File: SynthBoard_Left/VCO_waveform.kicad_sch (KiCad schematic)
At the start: 24 parts, among them IC6 AS321KTR-G1, IC7 HEF4013BT,653, Q1 2SC1623(RANGE:300-400)

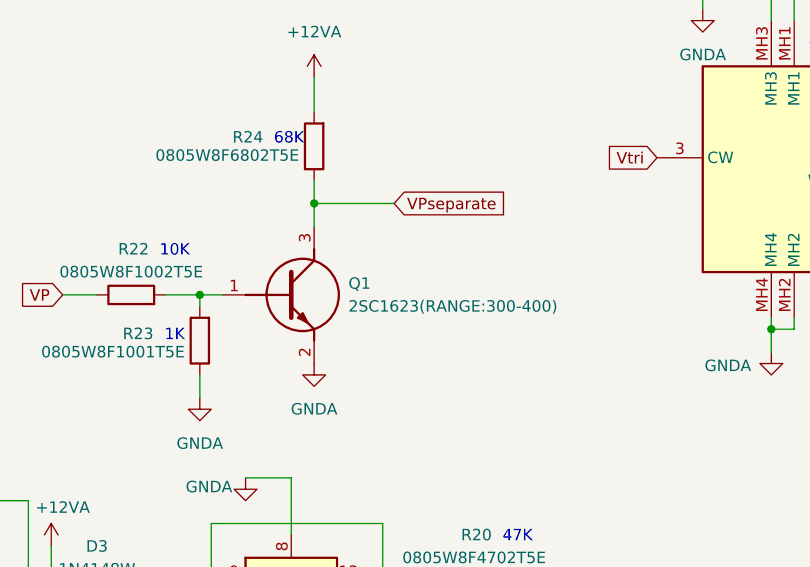
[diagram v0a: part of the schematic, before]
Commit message: SynthBoard_Left
JLCPCBでBasic部品に置き換えた
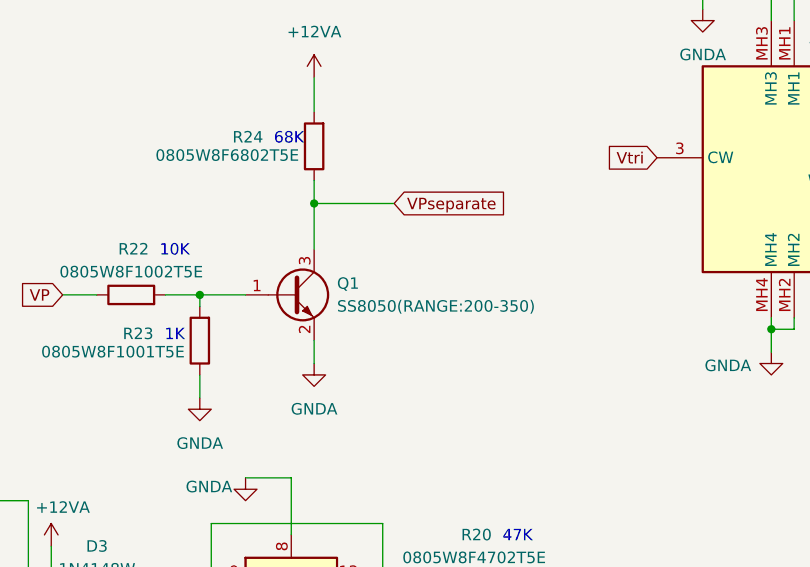
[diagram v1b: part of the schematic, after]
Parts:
- removed Q1: 2SC1623(RANGE:300-400), SamacSys_parts:SOT95P237X125-3N, symbol SamacSys_Parts:2SC1623-A
- added Q1: SS8050(RANGE:200-350), SamacSys_parts:SOT95P240X115-3N, symbol Transistor_BJT:SS8050
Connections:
- net GNDA: now also Q1.2 (E)
- net VPseparate: now also Q1.3 (C)
- net at R22.2, R23.2: now also Q1.1 (B)
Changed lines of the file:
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@@
 	(wire
 		(pts
-			(xy 105.41 90.17) (xy 105.41 92.71)
+			(xy 97.79 153.67) (xy 102.87 153.67)
 		)
 		(stroke
@@
 	(wire
 		(pts
-			(xy 97.79 153.67) (xy 102.87 153.67)
+			(xy 242.57 76.2) (xy 242.57 73.66)
 		)
 		(stroke
@@
 	(wire
 		(pts
-			(xy 242.57 76.2) (xy 242.57 73.66)
+			(xy 147.32 12.7) (xy 154.94 12.7)
 		)
 		(stroke
@@
 	(wire
 		(pts
-			(xy 147.32 12.7) (xy 154.94 12.7)
+			(xy 129.54 132.08) (xy 151.13 132.08)
 		)
 		(stroke
@@
 	(wire
 		(pts
-			(xy 129.54 132.08) (xy 151.13 132.08)
+			(xy 187.96 34.29) (xy 193.04 34.29)
 		)
 		(stroke
@@
 	(wire
 		(pts
-			(xy 187.96 34.29) (xy 193.04 34.29)
+			(xy 238.76 34.29) (xy 251.46 34.29)
 		)
 		(stroke
@@
 	(wire
 		(pts
-			(xy 238.76 34.29) (xy 251.46 34.29)
+			(xy 105.41 105.41) (xy 105.41 107.95)
 		)
 		(stroke
@@
 	(wire
 		(pts
-			(xy 92.71 100.33) (xy 95.25 100.33)
+			(xy 92.71 100.33) (xy 97.79 100.33)
 		)
 		(stroke
@@
 	(wire
 		(pts
+			(xy 105.41 90.17) (xy 105.41 95.25)
+		)
+		(stroke
+			(width 0)
+			(type default)
+		)
+	)
+	(wire
+		(pts
 			(xy 226.06 12.7) (xy 226.06 16.51)
 		)
@@
 	)
 	(symbol
-		(lib_id "SamacSys_Parts:2SC1623-A")
-		(at 95.25 100.33 0)
-		(unit 1)
-		(exclude_from_sim no)
-		(in_bom yes)
-		(on_board yes)
-		(dnp no)
-		(fields_autoplaced yes)
-		(property "Reference" "Q1"
-			(at 109.22 99.0599 0)
-			(effects
-				(font
-					(size 1.27 1.27)
-				)
-				(justify left)
-			)
-		)
-		(property "Value" "2SC1623(RANGE:300-400)"
-			(at 109.22 101.5999 0)
-			(effects
-				(font
-					(size 1.27 1.27)
-				)
-				(justify left)
-			)
-		)
-		(property "Footprint" "SamacSys_parts:SOT95P237X125-3N"
-			(at 109.22 201.6 0)
-			(effects
-				(font
-					(size 1.27 1.27)
-				)
-				(justify left top)
-				(hide yes)
-			)
-		)
-		(property "Datasheet" "https://www.mouser.in/datasheet/2/258/2SC1623_SOT_23_-1625845.pdf"
-			(at 109.22 301.6 0)
-			(effects
-				(font
-					(size 1.27 1.27)
-				)
-				(justify left top)
-				(hide yes)
-			)
-		)
-		(property "Description" "Renesas Electronics 2SC1623-A NPN Bipolar Transistor, 100 mA, 50 V, 3-Pin MiniMold"
-			(at 95.25 100.33 0)
-			(effects
-				(font
-					(size 1.27 1.27)
-				)
-				(hide yes)
-			)
-		)
-		(property "Height" "1.25"
-			(at 109.22 501.6 0)
-			(effects
-				(font
-					(size 1.27 1.27)
-				)
-				(justify left top)
-				(hide yes)
-			)
-		)
-		(property "Manufacturer_Name" "Renesas Electronics"
-			(at 109.22 601.6 0)
-			(effects
-				(font
-					(size 1.27 1.27)
-				)
-				(justify left top)
-				(hide yes)
-			)
-		)
-		(property "Manufacturer_Part_Number" "2SC1623-A"
-			(at 109.22 701.6 0)
-			(effects
-				(font
-					(size 1.27 1.27)
-				)
-				(justify left top)
-				(hide yes)
-			)
-		)
-		(property "Mouser Part Number" ""
-			(at 109.22 801.6 0)
-			(effects
-				(font
-					(size 1.27 1.27)
-				)
-				(justify left top)
-				(hide yes)
-			)
-		)
-		(property "Mouser Price/Stock" ""
-			(at 109.22 901.6 0)
-			(effects
-				(font
-					(size 1.27 1.27)
-				)
-				(justify left top)
-				(hide yes)
-			)
-		)
-		(property "Arrow Part Number" ""
-			(at 109.22 1001.6 0)
-			(effects
-				(font
-					(size 1.27 1.27)
-				)
-				(justify left top)
-				(hide yes)
-			)
-		)
-		(property "Arrow Price/Stock" ""
-			(at 109.22 1101.6 0)
-			(effects
-				(font
-					(size 1.27 1.27)
-				)
-				(justify left top)
-				(hide yes)
-			)
-		)
-		(pin "3"
-		)
-		(pin "2"
-		)
-		(pin "1"
-		)
-		(instances
-			(project "SynthBoard"
-				(path "/92765e2f-a998-485f-b610-76a9d5b50cba/54ae8d1b-caf5-4a85-9663-2a3f476f2243"
-					(reference "Q1")
-					(unit 1)
-				)
-			)
-		)
-	)
-	(symbol
 		(lib_id "SamacSys_Parts:PTA2043-2010CIB104")
 		(at 238.76 76.2 0)
@@
 					(unit 1)
 				)
+			)
+		)
+	)
+	(symbol
+		(lib_id "Transistor_BJT:SS8050")
+		(at 102.87 100.33 0)
+		(unit 1)
+		(exclude_from_sim no)
+		(in_bom yes)
+		(on_board yes)
+		(dnp no)
+		(fields_autoplaced yes)
+		(property "Reference" "Q1"
+			(at 107.95 99.0599 0)
+			(effects
+				(font
+					(size 1.27 1.27)
+				)
+				(justify left)
+			)
+		)
+		(property "Value" "SS8050(RANGE:200-350)"
+			(at 107.95 101.5999 0)
+			(effects
+				(font
+					(size 1.27 1.27)
+				)
+				(justify left)
+			)
+		)
+		(property "Footprint" "SamacSys_parts:SOT95P240X115-3N"
+			(at 107.95 107.696 0)
+			(effects
+				(font
+					(size 1.27 1.27)
+					(italic yes)
+				)
+				(justify left)
+				(hide yes)
+			)
+		)
+		(property "Datasheet" "http://www.secosgmbh.com/datasheet/products/SSMPTransistor/SOT-23/SS8050.pdf"
+			(at 107.95 105.156 0)
+			(effects
+				(font
+					(size 1.27 1.27)
+				)
+				(justify left)
+				(hide yes)
+			)
+		)
+		(property "Description" "General Purpose NPN Transistor, 1.5A Ic, 25V Vce, SOT-23"
+			(at 136.906 102.616 0)
+			(effects
+				(font
+					(size 1.27 1.27)
+				)
+				(hide yes)
+			)
+		)
+		(pin "1"
+		)
+		(pin "2"
+		)
+		(pin "3"
+		)
+		(instances
+			(project ""
+				(path "/92765e2f-a998-485f-b610-76a9d5b50cba/54ae8d1b-caf5-4a85-9663-2a3f476f2243"
+					(reference "Q1")
+					(unit 1)
+				)
